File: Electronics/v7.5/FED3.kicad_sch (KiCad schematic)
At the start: 33 parts, among them IC2 TB6612FNG, J2 Conn_01x02_Odd_Even, J3 USB4105-GF-A, SW1 Sw, U2 MIC5504-3.3, U3 MCP73834-xxxx, X3 B2B-PH-K-S

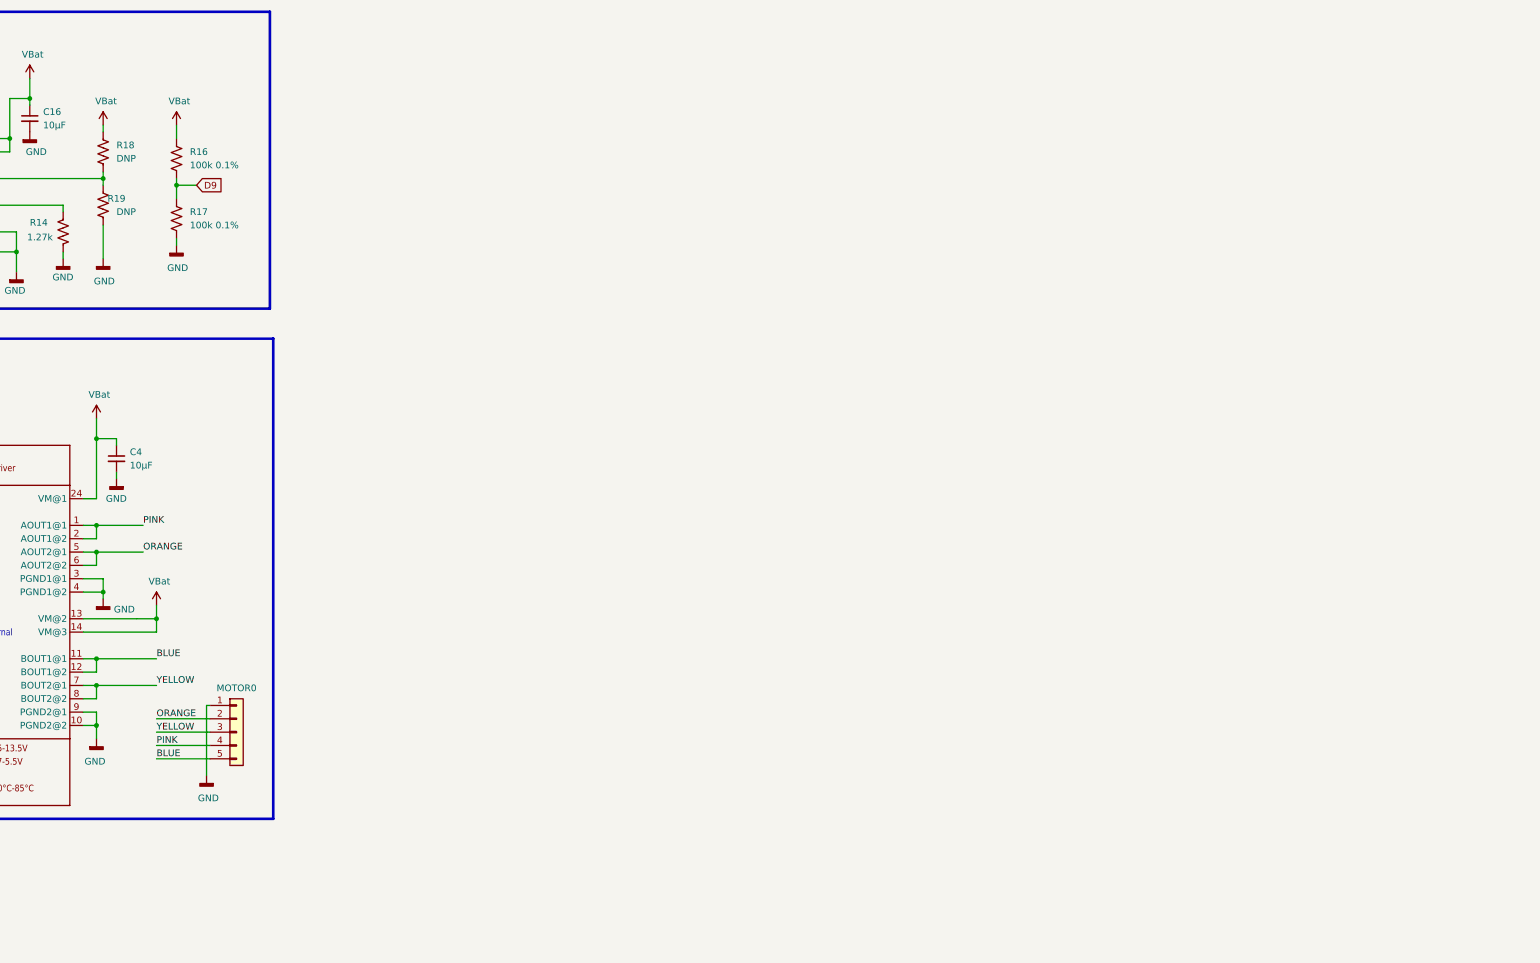
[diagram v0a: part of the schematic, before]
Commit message: Added battery comments to schematic.
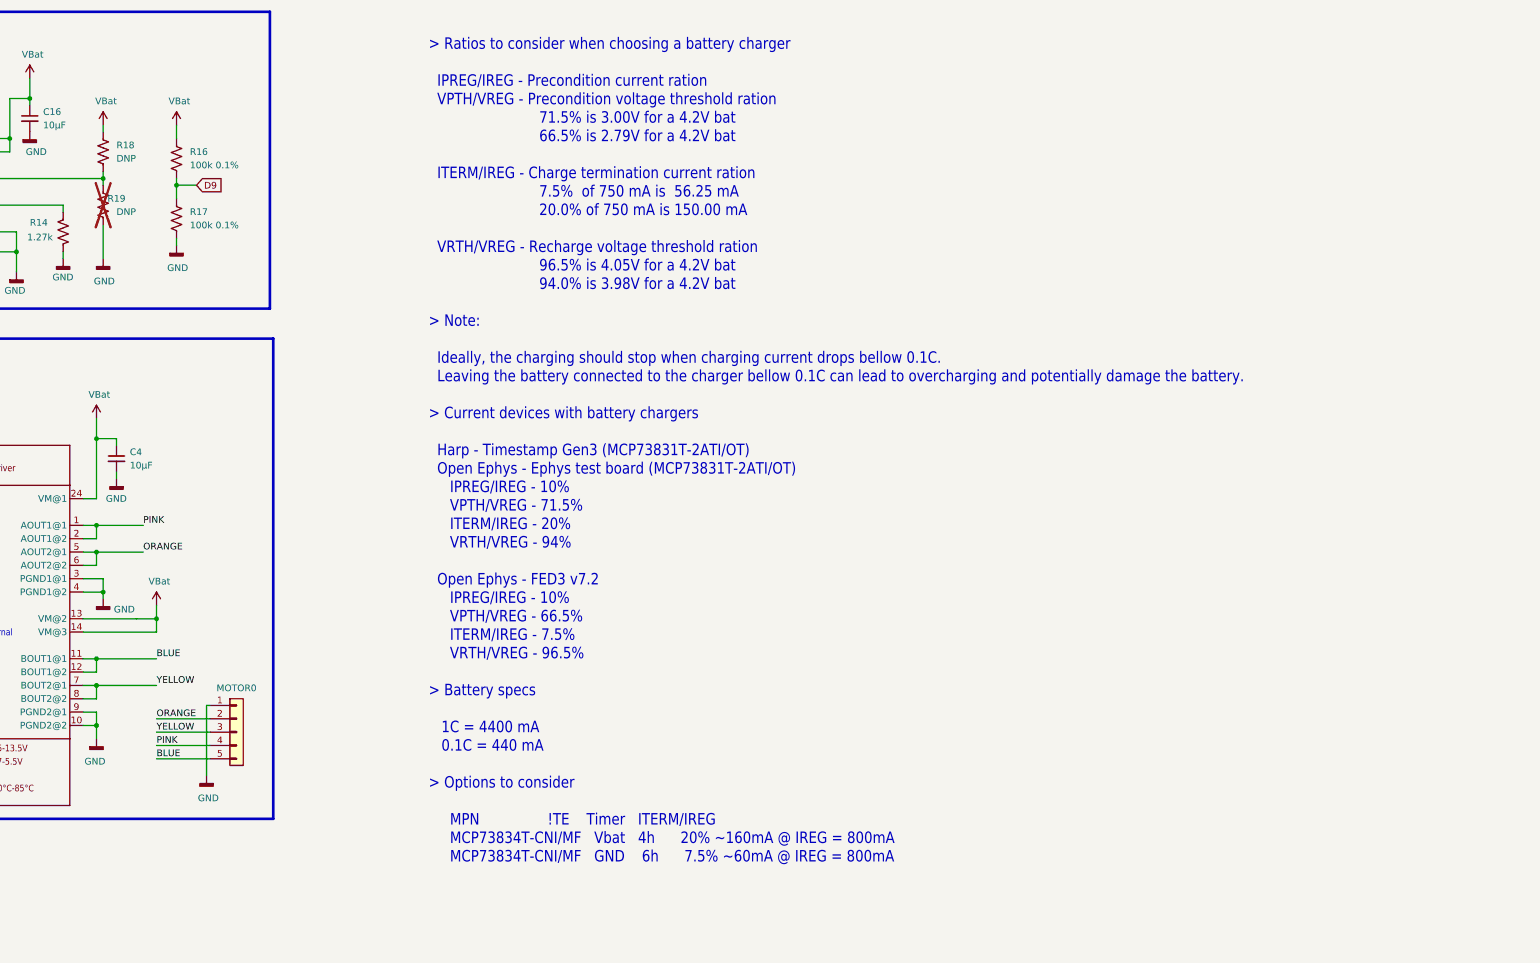
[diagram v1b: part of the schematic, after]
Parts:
- R19: now not fitted
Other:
- note added: "> Ratios to consider when choosing a battery charger IPREG/IREG - Precondition current ration VPTH/VREG - Precondition voltage threshold ration 71.5% is 3.00V for a 4.2V bat 66.5% is 2.79V for a 4.2V bat ITERM/IREG - Charge termination current ration 7.5% of 750 mA is 56.25 mA 20.0% of 750 mA is 150.00 mA VRTH/VREG - Recharge voltage threshold ration 96.5% is 4.05V for a 4.2V bat 94.0% is 3.98V f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"
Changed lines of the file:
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@@
 		)
 	)
+	(text "> Ratios to consider when choosing a battery charger\n\n  IPREG/IREG - Precondition current ration\n  VPTH/VREG - Precondition voltage threshold ration\n                          71.5% is 3.00V for a 4.2V bat\n                          66.5% is 2.79V for a 4.2V bat\n\n  ITERM/IREG - Charge termination current ration\n                          7.5%  of 750 mA is  56.25 mA\n                          20.0% of 750 mA is 150.00 mA\n\n  VRTH/VREG - Recharge voltage threshold ration\n                          96.5% is 4.05V for a 4.2V bat\n                          94.0% is 3.98V for a 4.2V bat\n\n> Note:\n\n  Ideally, the charging should stop when charging current drops bellow 0.1C.\n  Leaving the battery connected to the charger bellow 0.1C can lead to overcharging and potentially damage the battery.\n\n> Current devices with battery chargers\n\n  Harp - Timestamp Gen3 (MCP73831T-2ATI/OT)\n  Open Ephys - Ephys test board (MCP73831T-2ATI/OT)\n     IPREG/IREG - 10%\n     VPTH/VREG - 71.5%\n     ITERM/IREG - 20%\n     VRTH/VREG - 94%\n\n  Open Ephys - FED3 v7.2\n     IPREG/IREG - 10%\n     VPTH/VREG - 66.5%\n     ITERM/IREG - 7.5%\n     VRTH/VREG - 96.5%\n\n> Battery specs\n\n   1C = 4400 mA\n   0.1C = 440 mA\n\n> Options to consider\n\n     MPN                !TE    Timer   ITERM/IREG\n     MCP73834T-CNI/MF   Vbat   4h      20% ~160mA @ IREG = 800mA\n     MCP73834T-CNI/MF   GND    6h      7.5% ~60mA @ IREG = 800mA"
+		(exclude_from_sim no)
+		(at 300.736 176.276 0)
+		(effects
+			(font
+				(face "Consolas")
+				(size 2.1844 1.8567)
+				(thickness 0.2321)
+			)
+			(justify left bottom)
+		)
+	)
 	(text "LOW: Standby\n200 kΩ pull-down at internal"
 		(exclude_from_sim no)
@@
 		(in_bom yes)
 		(on_board yes)
-		(dnp no)
+		(dnp yes)
 		(property "Reference" "R19"
 			(at 241.3 49.5299 0)

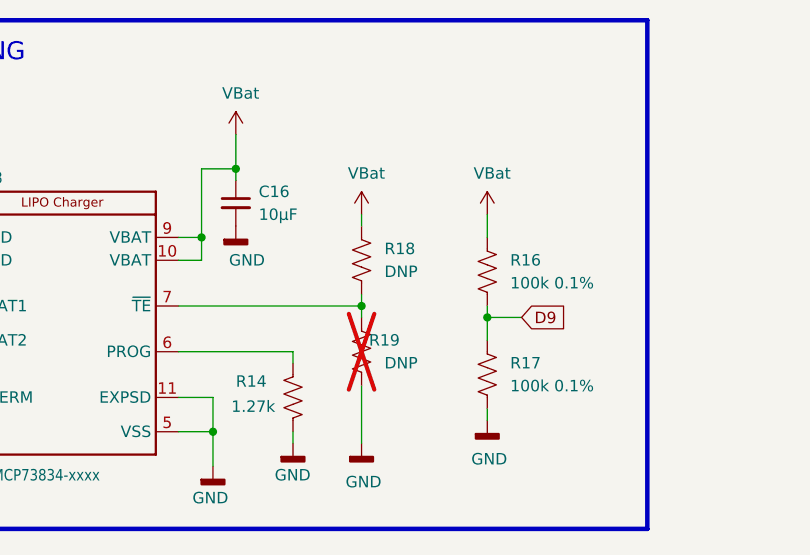
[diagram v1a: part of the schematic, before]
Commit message: Added MPN and OEPS PN to battery charger.
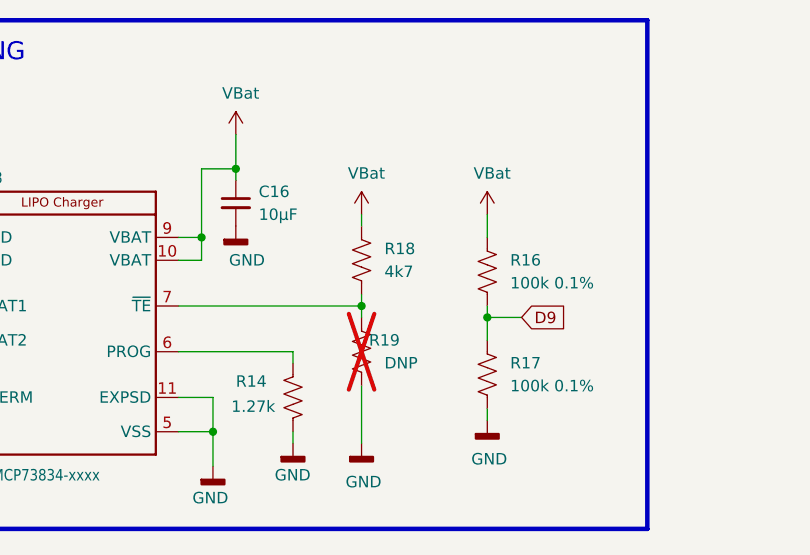
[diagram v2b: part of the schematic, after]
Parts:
- R18: value DNP -> 4k7; MPN n.a. -> ERJ-2RKF4701X; OEPSPN n.a. -> OEPS020010
- U3: MPN MCP73834-xxxx -> MCP73834-CNI/MF; OEPSPN _TBD -> OEPS080177
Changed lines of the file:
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@@
 			)
 		)
-		(property "Value" "DNP"
+		(property "Value" "4k7"
 			(at 241.3 41.9099 0)
 			(effects
@@
 			)
 		)
-		(property "Description" ""
+		(property "Description" "SMD 0402 4k7"
 			(at 238.76 40.64 0)
 			(effects
@@
 			)
 		)
-		(property "OEPSPN" "n.a."
+		(property "OEPSPN" "OEPS020010"
 			(at 238.76 40.64 0)
 			(effects
@@
 			)
 		)
-		(property "MPN" "n.a."
+		(property "MPN" "ERJ-2RKF4701X"
 			(at 238.76 40.64 0)
 			(effects
@@
 			)
 		)
-		(property "Description" "SMD 0402 1kΩ ±1% 0.100W"
+		(property "Description" "SMD 0402 4k7"
 			(at 175.26 41.91 0)
 			(effects
@@
 			)
 		)
-		(property "OEPSPN" "_TBD"
+		(property "OEPSPN" "OEPS080177"
 			(at 205.74 40.64 0)
 			(effects
@@
 			)
 		)
-		(property "MPN" "MCP73834-xxxx"
+		(property "MPN" "MCP73834-CNI/MF"
 			(at 205.74 40.64 0)
 			(effects

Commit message: Added MPN and OEPS PN to remaining components.
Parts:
- MOTOR0: MPN n.a. -> M20-9990546; OEPSPN n.a. -> OEPS070131
- R19, R7: OEPSPN n.a. -> OEPS00000
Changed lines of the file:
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@@
 			)
 		)
-		(property "OEPSPN" "n.a."
+		(property "OEPSPN" "OEPS00000"
 			(at 238.76 50.8 0)
 			(effects
@@
 			)
 		)
-		(property "OEPSPN" "n.a."
+		(property "OEPSPN" "OEPS00000"
 			(at 180.34 120.65 0)
 			(effects
@@
 			)
 		)
-		(property "OEPSPN" "n.a."
+		(property "OEPSPN" "OEPS070131"
 			(at 264.16 151.13 0)
 			(effects
@@
 			)
 		)
-		(property "MPN" "n.a."
+		(property "MPN" "M20-9990546"
 			(at 264.16 151.13 0)
 			(effects

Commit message: Fixed OEPS PN of the DNP components.
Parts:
- R19, R7: OEPSPN OEPS00000 -> OEPS000000
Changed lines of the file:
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@@
 			)
 		)
-		(property "OEPSPN" "OEPS00000"
+		(property "OEPSPN" "OEPS000000"
 			(at 238.76 50.8 0)
 			(effects
@@
 			)
 		)
-		(property "OEPSPN" "OEPS00000"
+		(property "OEPSPN" "OEPS000000"
 			(at 180.34 120.65 0)
 			(effects
